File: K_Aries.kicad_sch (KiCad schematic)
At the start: 0 parts

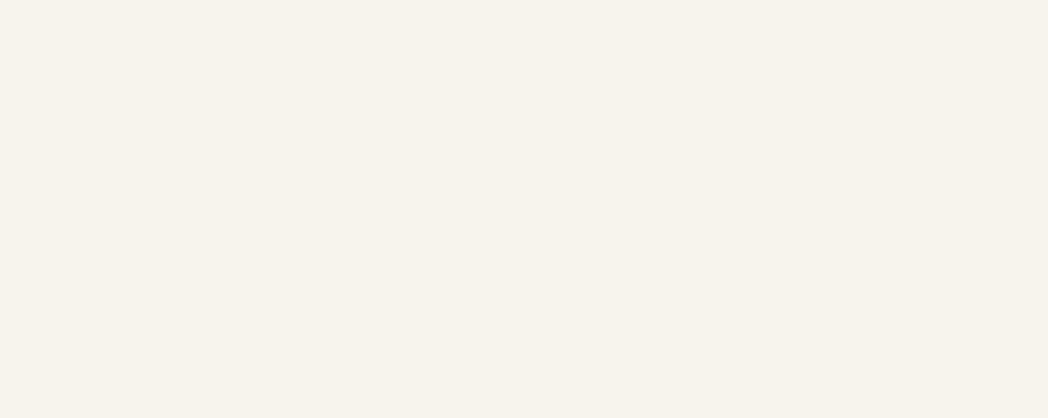
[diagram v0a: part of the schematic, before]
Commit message: schematic fully captured
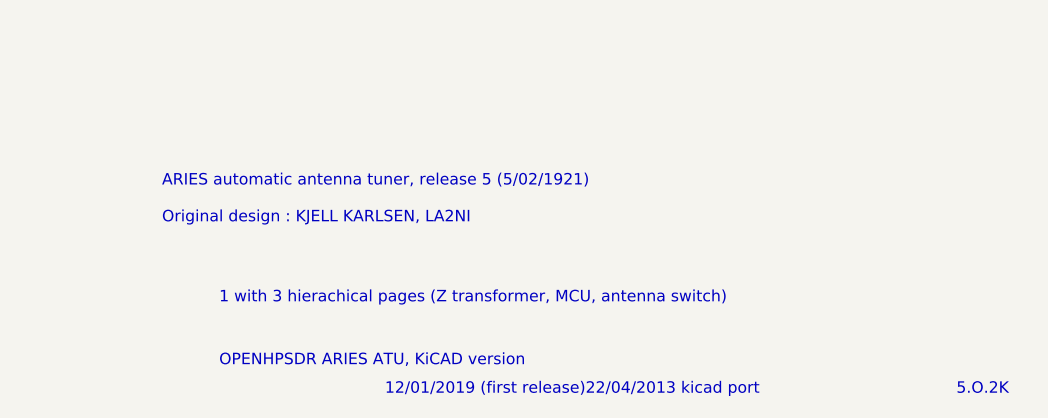
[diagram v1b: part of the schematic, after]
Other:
- note added: "1 with 3 hierachical pages (Z transformer, MCU, antenna switch)"
- note added: "12/01/2019 (first release)22/04/2013 kicad port"
- note added: "5.O.2K"
- note added: "ARIES automatic antenna tuner, release 5 (5/02/1921) Original design : KJELL KARLSEN, LA2NI"
- note added: "OPENHPSDR ARIES ATU, KiCAD version"
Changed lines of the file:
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@@
 (kicad_sch (version 20230121) (generator eeschema)
   (paper "A4")
+  (text "OPENHPSDR ARIES ATU, KiCAD version" (at 187.96 190.5 0)
+    (effects (font (size 1.27 1.27)) (justify left bottom))
+  )
+  (text "12/01/2019 (first release)22/04/2013 kicad port\n" (at 206.375 193.675 0)
+    (effects (font (size 1.27 1.27)) (justify left bottom))
+  )
+  (text "\nARIES automatic antenna tuner, release 5 (5/02/1921)\n\nOriginal design : KJELL KARLSEN, LA2NI"
+    (at 181.61 174.625 0)
+    (effects (font (size 1.27 1.27)) (justify left bottom))
+  )
+  (text "1 with 3 hierachical pages (Z transformer, MCU, antenna switch)"
+    (at 187.96 183.515 0)
+    (effects (font (size 1.27 1.27)) (justify left bottom))
+  )
+  (text "5.O.2K" (at 269.875 193.675 0)
+    (effects (font (size 1.27 1.27)) (justify left bottom))
+  )
   (sheet (at 27.305 135.89) (size 91.44 43.18) (fields_autoplaced)
     (stroke (width 0.1524) (type solid))
